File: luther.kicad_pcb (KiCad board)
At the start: 2 copper layers, 114 x 50 mm, 2 parts

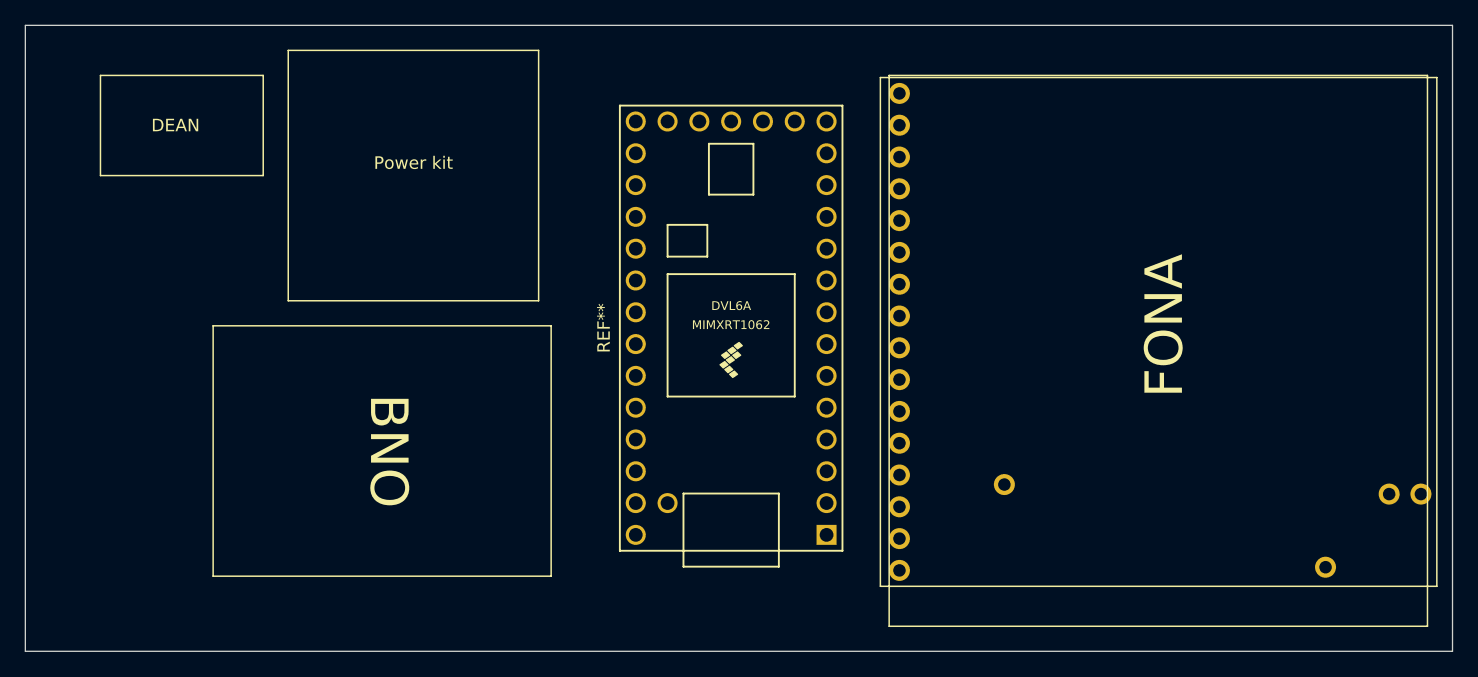
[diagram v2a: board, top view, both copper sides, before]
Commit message: add schema for lora, teensy, fona
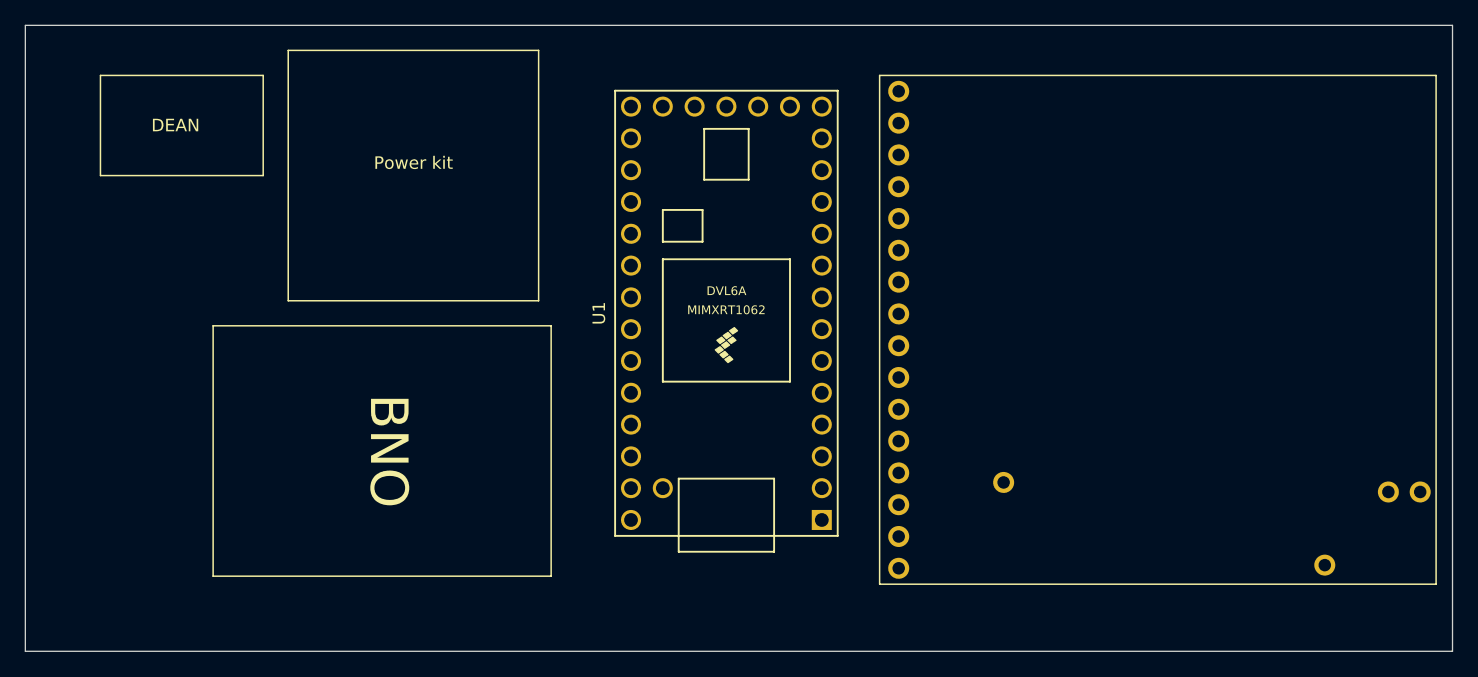
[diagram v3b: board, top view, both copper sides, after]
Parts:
- removed REF**: Teensy4.0, libs:Teensy40
- added U1: Teensy4.0, NUSTARS Libs:Teensy40, F.Cu at (86.0, 93.0)
- 1: value FONA808 -> FONA808_FONA808
- moved 1 0.18 mm to (99.0, 74.0)
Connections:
- 1 pad 1: (no net) -> 5V
- 1 pad 10: (no net) -> Net-(1-Pad10)
- 1 pad 11: (no net) -> Net-(1-Pad11)
- 1 pad 12: (no net) -> Net-(1-Pad12)
- 1 pad 13: (no net) -> Net-(1-Pad13)
- 1 pad 14: (no net) -> Net-(1-Pad14)
- 1 pad 15: (no net) -> Net-(1-Pad15)
- 1 pad 16: (no net) -> Net-(1-Pad16)
- 1 pad 17: (no net) -> Net-(1-Pad17)
- 1 pad 18: (no net) -> Net-(1-Pad18)
- 1 pad 19: (no net) -> Net-(1-Pad19)
- 1 pad 2: (no net) -> Net-(1-Pad2)
- 1 pad 20: (no net) -> Net-(1-Pad20)
- 1 pad 3: (no net) -> Net-(1-Pad3)
- 1 pad 4: (no net) -> 3V3T
- 1 pad 5: (no net) -> Net-(1-Pad5)
- 1 pad 6: (no net) -> T2FNA
- 1 pad 7: (no net) -> FNA2T
- 1 pad 8: (no net) -> Net-(1-Pad8)
- 1 pad 9: (no net) -> GND
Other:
- board text removed: "FONA"
